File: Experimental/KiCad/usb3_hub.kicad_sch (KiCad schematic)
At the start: 74 parts, among them IC10 TPS62933ODRLR, IC11 FUSB303BTMX, IC12 TPS2069E, IC9 USB5816C-I/KD, X6 USB4056-03-A, Y2 ABM8-25.000MHZ-D2X-T

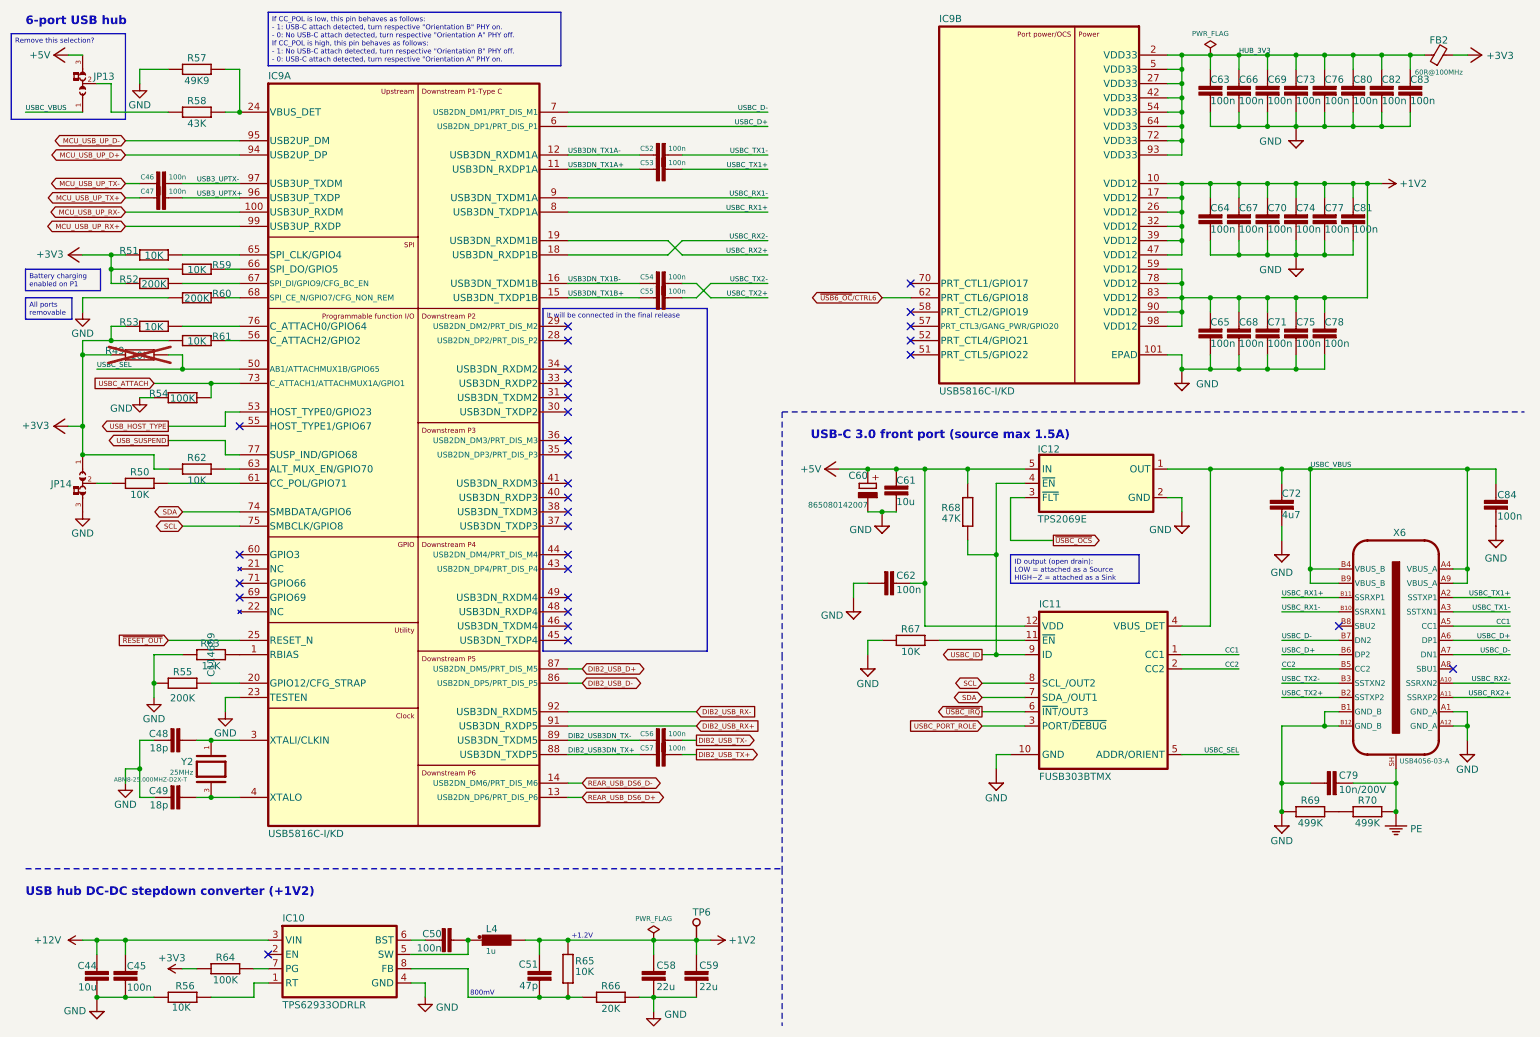
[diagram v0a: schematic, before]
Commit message: BOM update, small changes
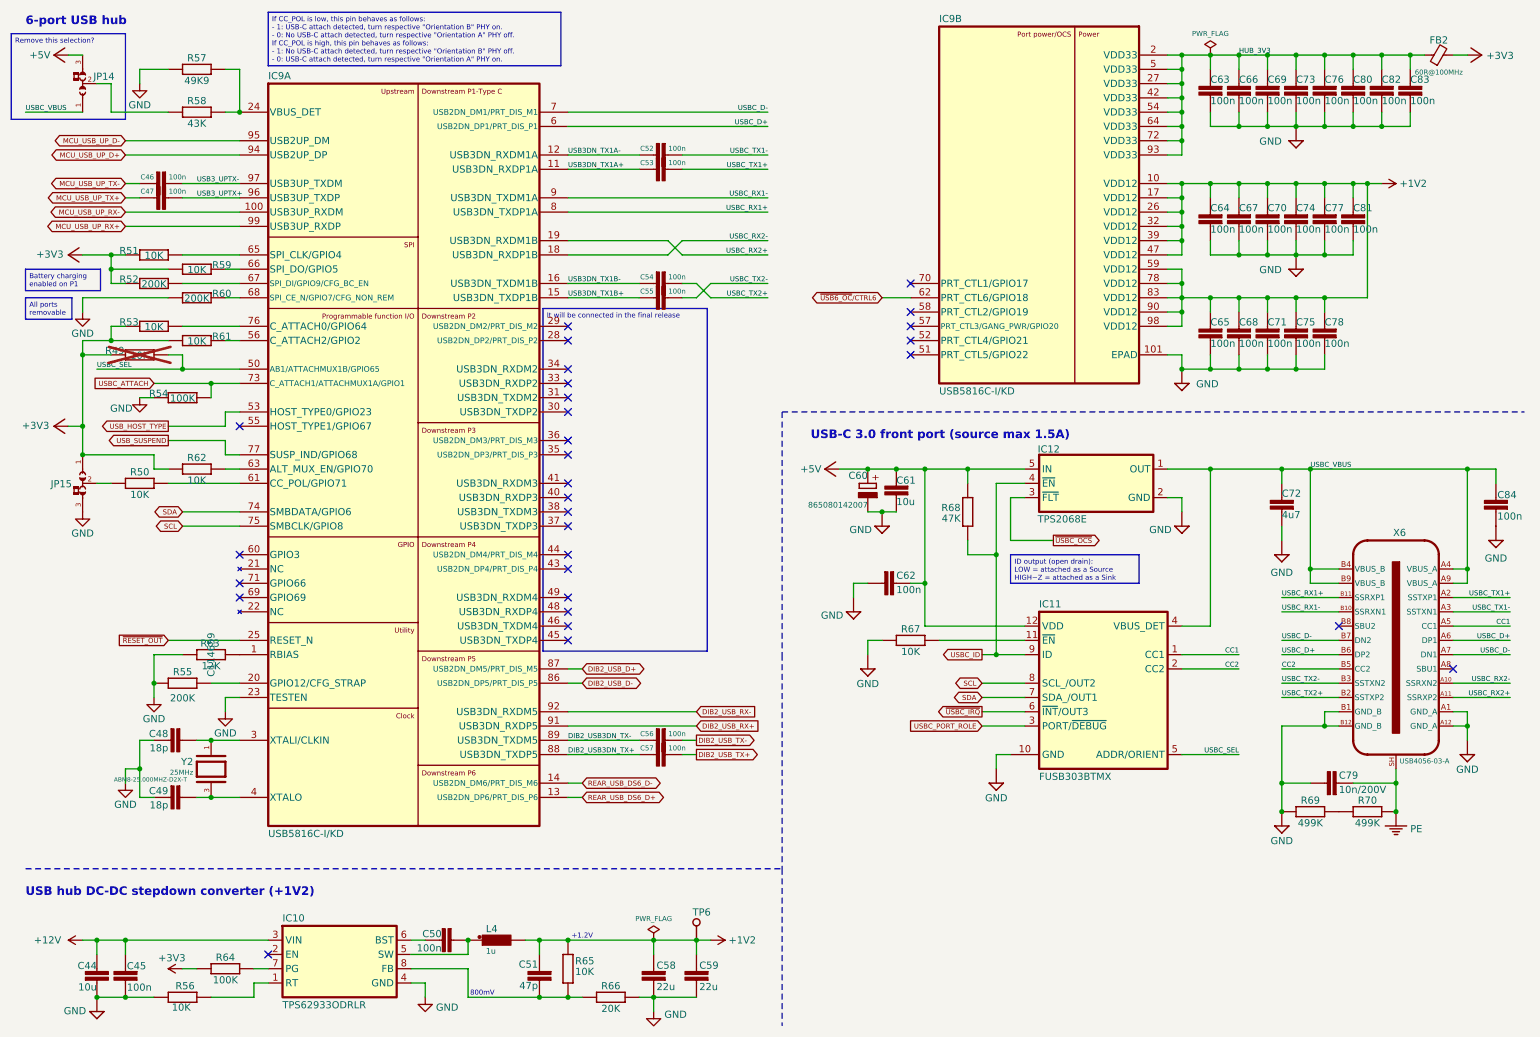
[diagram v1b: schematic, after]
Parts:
- IC12: value TPS2069E -> TPS2068E
- R52, R55, R60: TME SMD0603-3K3-1% -> SMD0603-200K-1%
- renumbered JP13 to JP14, JP14 to JP15
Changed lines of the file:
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@@
 	(title_block
 		(title "BB3+ test mainboard")
-		(date "2025-10-11")
+		(date "2025-10-12")
 		(rev "r1B1")
 		(company "Envox d.o.o.")
@@
 			)
 		)
-		(property "TME" "SMD0603-3K3-1%"
+		(property "TME" "SMD0603-200K-1%"
 			(at 38.1 63.5 0)
 			(effects
@@
 			)
 		)
-		(property "Value" "TPS2069E"
+		(property "Value" "TPS2068E"
 			(at 195.326 106.172 0)
 			(effects
@@
 		(on_board yes)
 		(dnp no)
-		(property "Reference" "#SUPPLY050"
+		(property "Reference" "#SUPPLY051"
 			(at 241.3 60.96 0)
 			(effects
@@
 			(project "BB3plus MCU test board"
 				(path "/1df84e4f-233a-4f72-9418-c0020706bb76/99b67fa5-56ce-4798-a21a-d86c3d347c55"
-					(reference "#SUPPLY050")
+					(reference "#SUPPLY051")
 					(unit 1)
 				)
@@
 			)
 		)
-		(property "TME" "SMD0603-3K3-1%"
+		(property "TME" "SMD0603-200K-1%"
 			(at 45.72 66.04 0)
 			(effects
@@
 		(on_board yes)
 		(dnp no)
-		(property "Reference" "#SUPPLY049"
+		(property "Reference" "#SUPPLY050"
 			(at 241.3 38.1 0)
 			(effects
@@
 			(project "BB3plus MCU test board"
 				(path "/1df84e4f-233a-4f72-9418-c0020706bb76/99b67fa5-56ce-4798-a21a-d86c3d347c55"
-					(reference "#SUPPLY049")
+					(reference "#SUPPLY050")
 					(unit 1)
 				)
@@
 		(on_board yes)
 		(dnp no)
-		(property "Reference" "#SUPPLY048"
+		(property "Reference" "#SUPPLY049"
 			(at 220.98 81.28 0)
 			(effects
@@
 			(project "BB3plus MCU test board"
 				(path "/1df84e4f-233a-4f72-9418-c0020706bb76/99b67fa5-56ce-4798-a21a-d86c3d347c55"
-					(reference "#SUPPLY048")
+					(reference "#SUPPLY049")
 					(unit 1)
 				)
@@
 		(on_board yes)
 		(dnp no)
-		(property "Reference" "JP14"
+		(property "Reference" "JP15"
 			(at 23.495 98.425 90)
 			(effects
@@
 			(project "BB3plus MCU test board"
 				(path "/1df84e4f-233a-4f72-9418-c0020706bb76/99b67fa5-56ce-4798-a21a-d86c3d347c55"
-					(reference "JP14")
+					(reference "JP15")
 					(unit 1)
 				)
@@
 		(on_board yes)
 		(dnp no)
-		(property "Reference" "#SUPPLY047"
+		(property "Reference" "#SUPPLY048"
 			(at 127 193.04 0)
 			(effects
@@
 			(project "BB3plus MCU test board"
 				(path "/1df84e4f-233a-4f72-9418-c0020706bb76/99b67fa5-56ce-4798-a21a-d86c3d347c55"
-					(reference "#SUPPLY047")
+					(reference "#SUPPLY048")
 					(unit 1)
 				)
@@
 		(on_board yes)
 		(dnp no)
-		(property "Reference" "JP13"
+		(property "Reference" "JP14"
 			(at 27.305 26.67 90)
 			(effects
@@
 			(project "BB3plus MCU test board"
 				(path "/1df84e4f-233a-4f72-9418-c0020706bb76/99b67fa5-56ce-4798-a21a-d86c3d347c55"
-					(reference "JP13")
+					(reference "JP14")
 					(unit 1)
 				)
@@
 		(on_board yes)
 		(dnp no)
-		(property "Reference" "#SUPPLY046"
+		(property "Reference" "#SUPPLY047"
 			(at 86.36 190.5 0)
 			(effects
@@
 			(project "BB3plus MCU test board"
 				(path "/1df84e4f-233a-4f72-9418-c0020706bb76/99b67fa5-56ce-4798-a21a-d86c3d347c55"
-					(reference "#SUPPLY046")
+					(reference "#SUPPLY047")
 					(unit 1)
 				)
@@
 		(on_board yes)
 		(dnp no)
-		(property "Reference" "#SUPPLY045"
+		(property "Reference" "#SUPPLY046"
 			(at 27.94 193.04 0)
 			(effects
@@
 			(project "BB3plus MCU test board"
 				(path "/1df84e4f-233a-4f72-9418-c0020706bb76/99b67fa5-56ce-4798-a21a-d86c3d347c55"
-					(reference "#SUPPLY045")
+					(reference "#SUPPLY046")
 					(unit 1)
 				)
@@
 			)
 		)
-		(property "TME" "SMD0603-3K3-1%"
+		(property "TME" "SMD0603-200K-1%"
 			(at 43.18 134.62 0)
 			(effects

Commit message: Replace 5V buck with 6A low EMI version
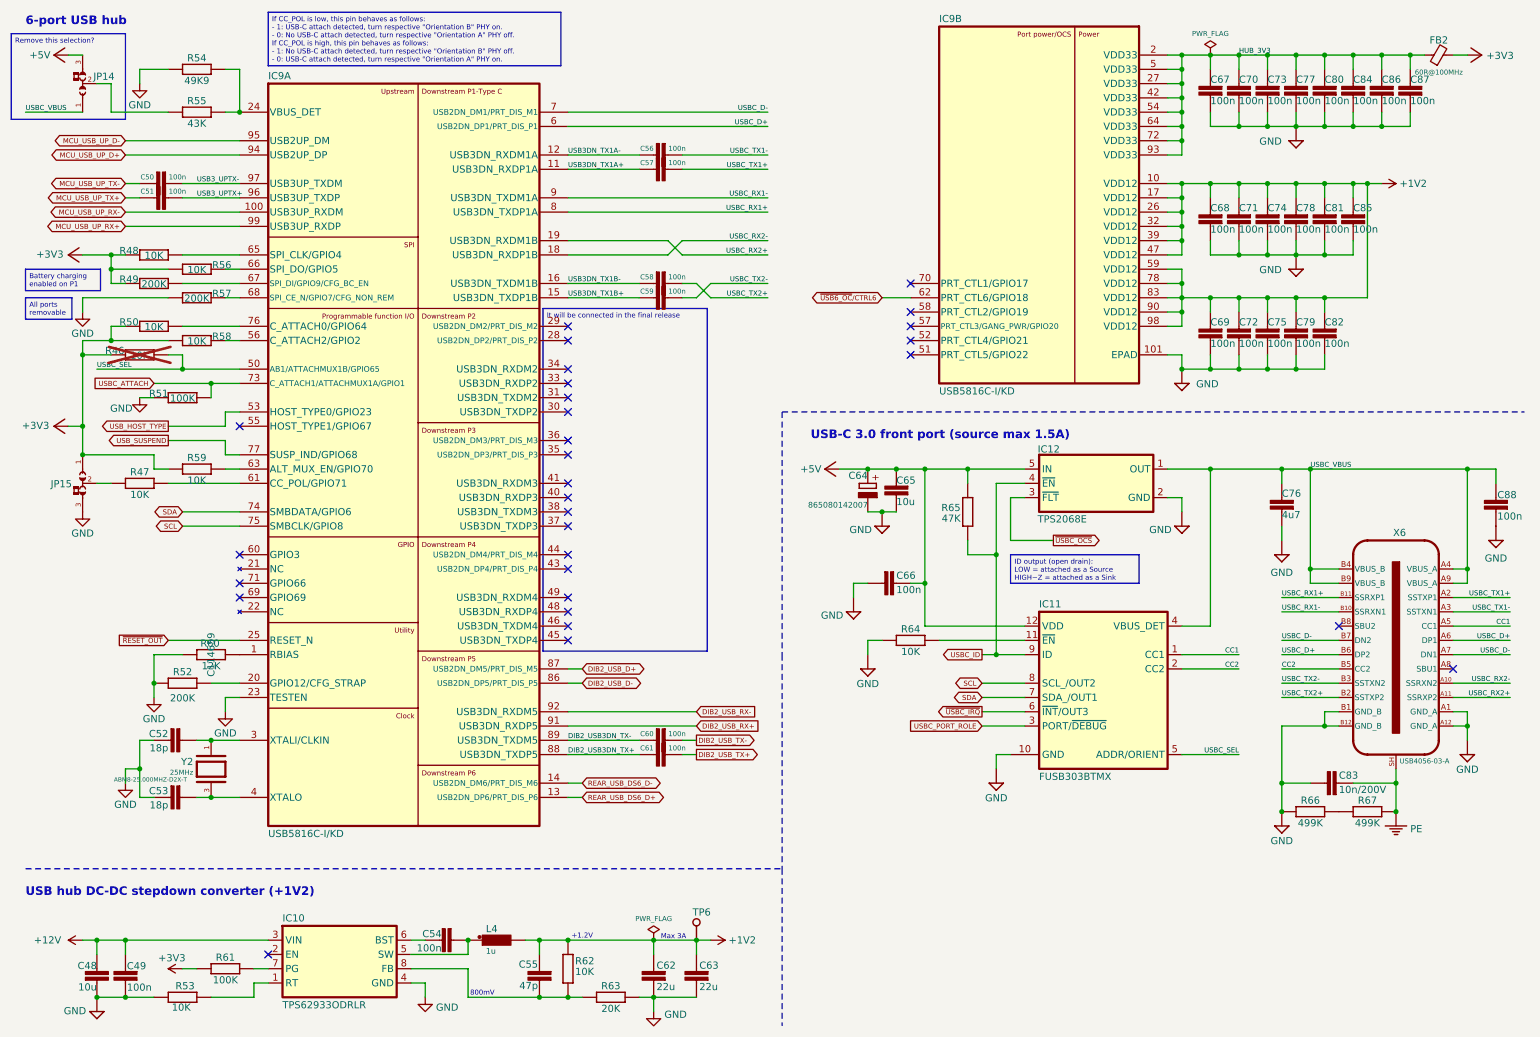
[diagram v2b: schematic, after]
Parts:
- IC10: symbol PCM_Uvitron:TPS62933ODRLR -> PCM_EEZ_TI:TPS62933ODRLR
- renumbered C44 to C48, C45 to C49, C46 to C50, C47 to C51, C48 to C52, C49 to C53, C50 to C54, C51 to C55, C52 to C56, C53 to C57, C54 to C58, C55 to C59, C56 to C60, C57 to C61, C58 to C62, C59 to C63, C60 to C64, C61 to C65, C62 to C66, C63 to C67, C64 to C68, C65 to C69, C66 to C70, C67 to C71, C68 to C72, C69 to C73, C70 to C74, C71 to C75, C72 to C76, C73 to C77, C74 to C78, C75 to C79, C76 to C80, C77 to C81, C78 to C82, C79 to C83, C80 to C84, C81 to C85, C82 to C86, C83 to C87, C84 to C88, R49 to R46, R50 to R47, R51 to R48, R52 to R49, R53 to R50, R54 to R51, R55 to R52, R56 to R53, R57 to R54, R58 to R55, R59 to R56, R60 to R57, R61 to R58, R62 to R59, R63 to R60, R64 to R61, R65 to R62, R66 to R63, R67 to R64, R68 to R65, R69 to R66, R70 to R67
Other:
- note added: "Max 3A"

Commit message: Update project info
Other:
- company: Envox d.o.o. -> ${project_creator}
- title: BB3+ test mainboard -> ${project_name}
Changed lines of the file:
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@@
 	(paper "A4")
 	(title_block
-		(title "BB3+ test mainboard")
-		(date "2025-10-12")
-		(rev "r1B1")
-		(company "Envox d.o.o.")
-		(comment 1 "Licensed under the TAPR Open Hardware License (www.tapr.org/OHL)")
-		(comment 2 "More info at http://www.envox.eu/")
+		(title "${project_name}")
+		(date "2025-10-13")
+		(rev "${project_version}")
+		(company "${project_creator}")
+		(comment 1 "${project_license}")
+		(comment 2 "${project_info}")
 	)
 	(text "Max 3A"

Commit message: Output LC filters added on all buck converters
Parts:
- added C66: 22u, PCM_EEZ_passives:C_0805_2012Metric, symbol PCM_EEZ_passives:C-EU
- added FB4: BLE18PS080SN1D, PCM_EEZ_passives:BEAD0603, symbol PCM_EEZ_passives:L_Ferrite Bead
- renumbered C48 to C50, C49 to C51, C50 to C52, C51 to C53, C52 to C54, C53 to C55, C54 to C56, C55 to C57, C56 to C58, C57 to C59, C58 to C60, C59 to C61, C60 to C62, C61 to C63, C62 to C64, C63 to C65, C64 to C67, C65 to C68, C66 to C69, C67 to C70, C68 to C71, C69 to C72, C70 to C73, C71 to C74, C72 to C75, C73 to C76, C74 to C77, C75 to C78, C76 to C79, C77 to C80, C78 to C81, C79 to C82, C80 to C83, C81 to C84, C82 to C85, C83 to C86, C84 to C87, C85 to C88, C86 to C89, C87 to C90, C88 to C91, FB2 to FB5
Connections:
- net +1V2: now also C66.2, FB4.2; no longer C57.1, C64.2, C65.2, L4.2, R62.2
- net GND: now also C66.1
- new net +1V2out: C57.1, C64.2, C65.2, FB4.1, L4.2, R62.2
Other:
- note added: "+800mV"
- note removed: "800mV"
- moved on the sheet: TP6

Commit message: Various small fixes
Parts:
- renumbered R46 to R47, R47 to R48, R48 to R49, R49 to R50, R50 to R51, R51 to R52, R52 to R53, R53 to R54, R54 to R55, R55 to R56, R56 to R57, R57 to R58, R58 to R59, R59 to R60, R60 to R61, R61 to R62, R62 to R63, R63 to R64, R64 to R65, R65 to R66, R66 to R67, R67 to R68
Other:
- note added: "DIB #3"
- note added: "DIB #4"
- note added: "DIB #5"

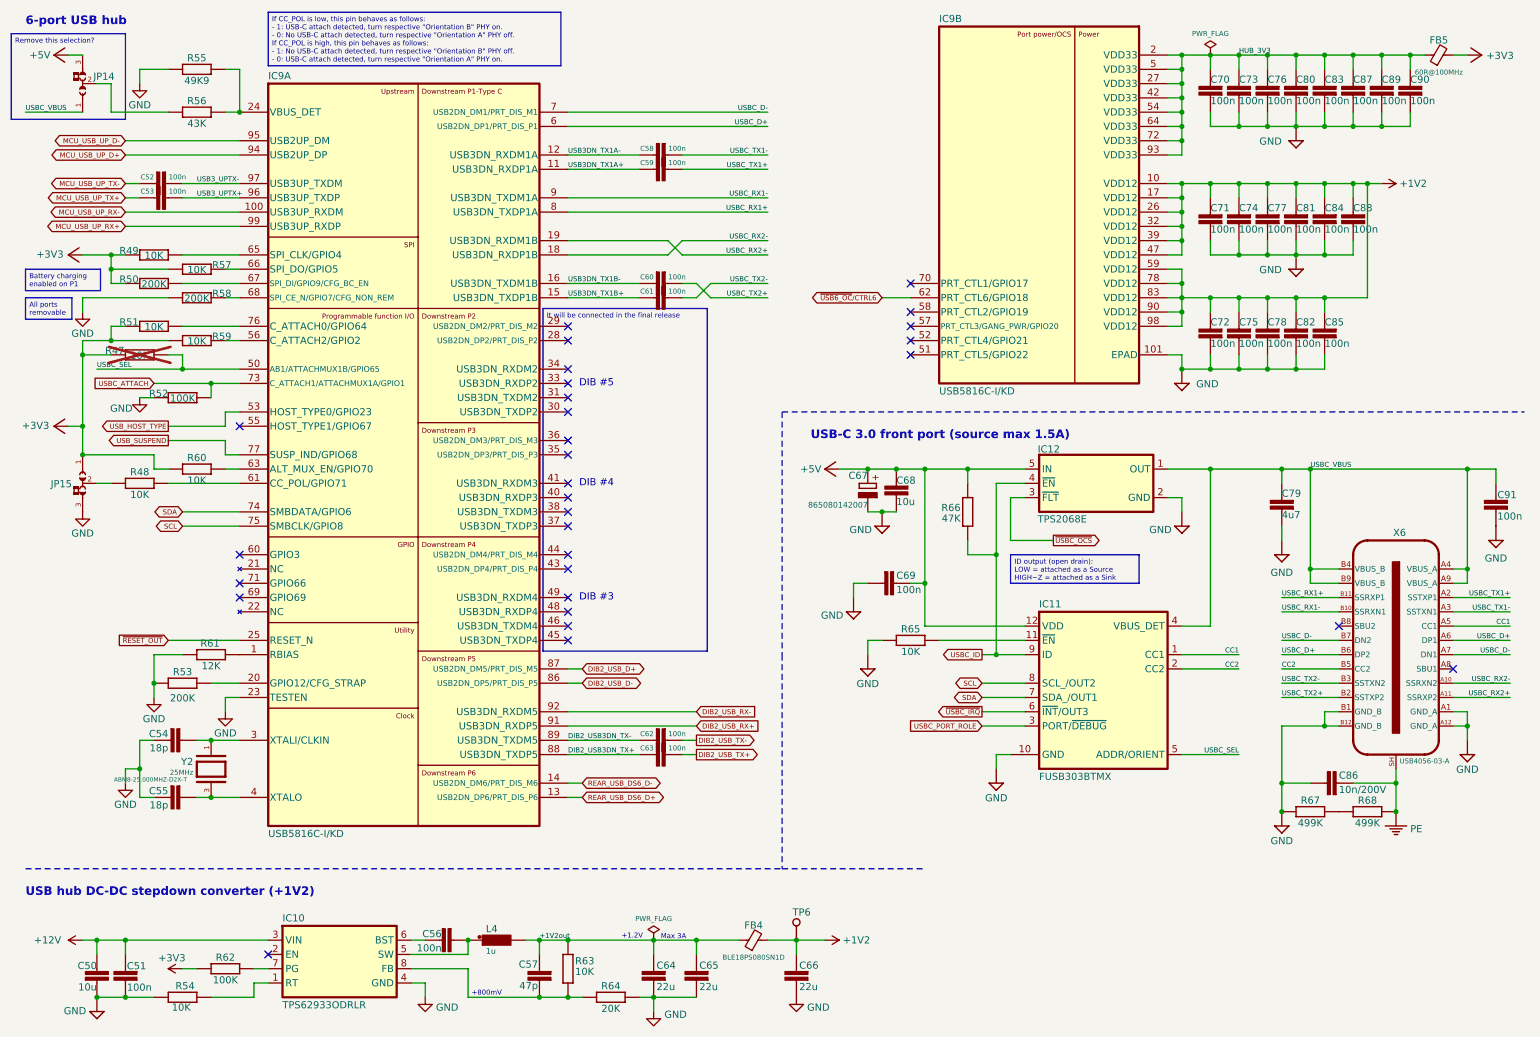
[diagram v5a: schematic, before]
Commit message: Hub section corrections in collaboration with Microchip support
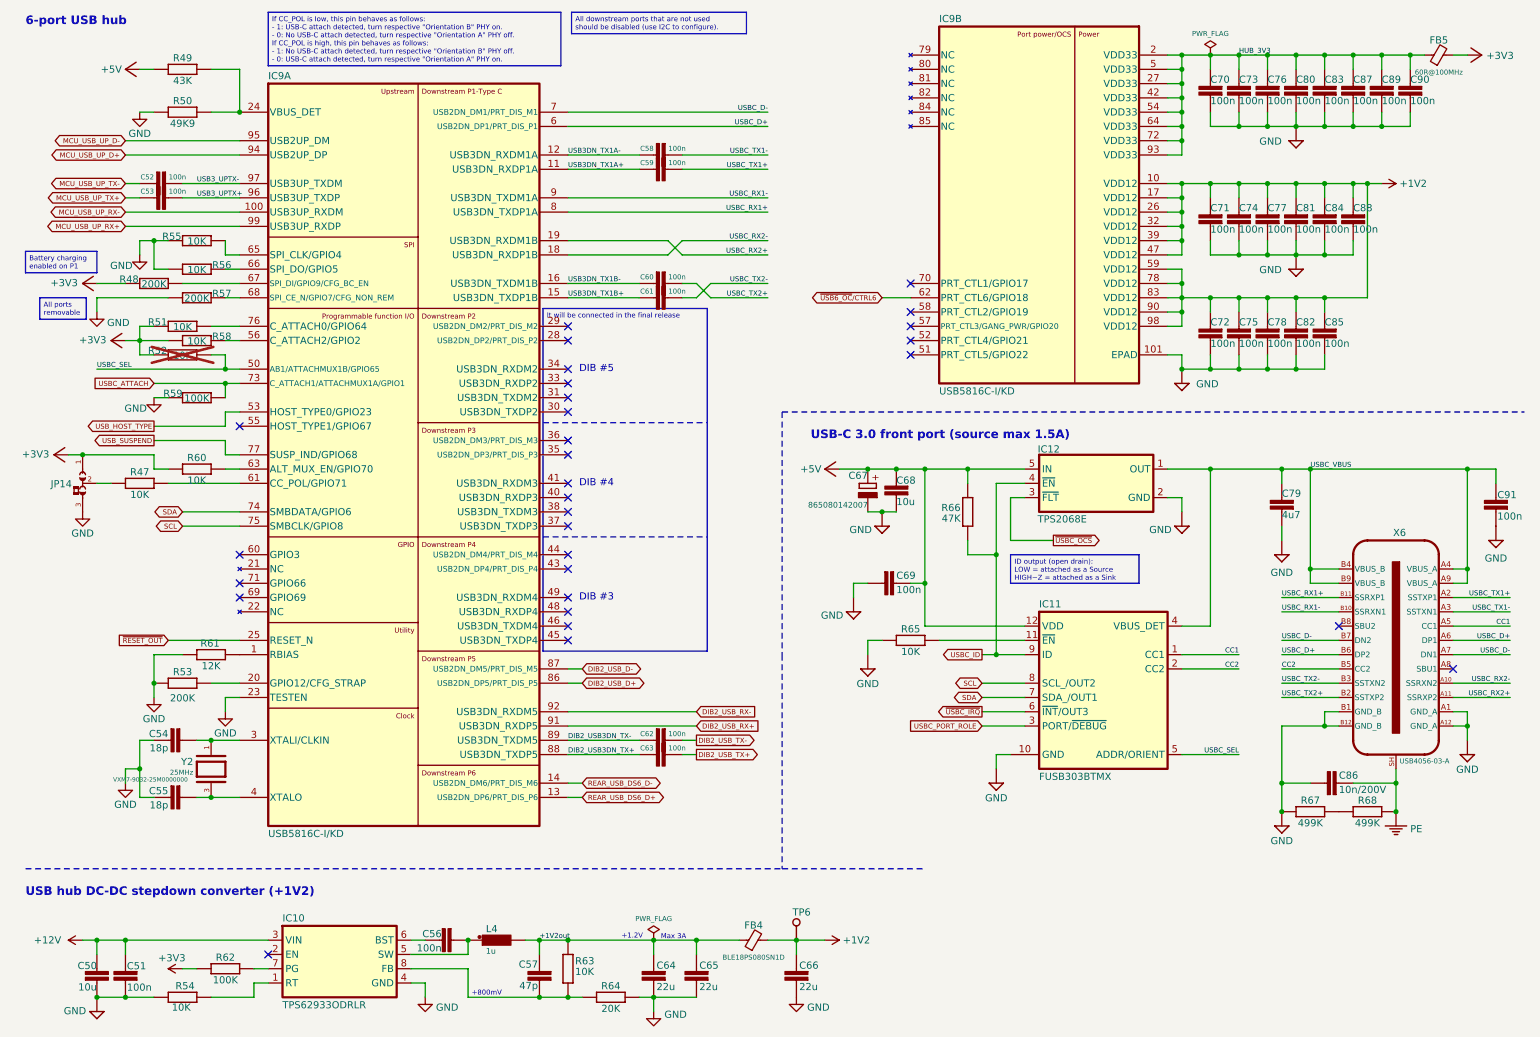
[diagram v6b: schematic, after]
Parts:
- removed JP14: ~, PCM_EEZ_SMD:JP3 shorted with 0R (0603) 2-3, symbol PCM_EEZ_unsorted:JP3 shorted with 0R (2-3)
- Y2: value ABM8-25.000MHZ-D2X-T -> VXM7-9032-25M0000000; DigiKey 535-14398-1-ND -> 150-VXM7-9032-25M0000000CT-ND; LCSC C1986777 -> C1517995; Mouser 815-ABM825MHZD2XT -> 579-M7903225M0000000; TME 325G-25.000MDDJ-T -> -
- renumbered JP15 to JP14, R48 to R47, R50 to R48, R56 to R49, R55 to R50, R47 to R52, R49 to R55, R57 to R56, R58 to R57, R59 to R58, R52 to R59
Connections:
- net +3V3: no longer R55.2, R56.2
- net +5V: now also R49.1
- net DIB2_USB_D+: now also IC9.86 (USB2DN_DP5/PRT_DIS_P5); no longer IC9.87 (USB2DN_DM5/PRT_DIS_M5)
- net DIB2_USB_D-: now also IC9.87 (USB2DN_DM5/PRT_DIS_M5); no longer IC9.86 (USB2DN_DP5/PRT_DIS_P5)
- net GND: now also R55.2, R56.2
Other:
- moved on the sheet: R49, R50, R51, R52, R55, R59
